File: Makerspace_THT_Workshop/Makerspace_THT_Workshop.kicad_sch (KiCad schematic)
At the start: 22 parts, among them SW1 SW_SPDT, U1 LM358, U2 LMC555xN

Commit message: Updated the board to fix alot of stuff
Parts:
- removed D2: LED, LED_THT:LED_D5.0mm_5.0mm_Pitch, symbol Device:LED
- removed R10: 100, Resistor_THT:R_Axial_DIN0207_L6.3mm_D2.5mm_P7.62mm_Horizontal, symbol Device:R
- AE1: footprint Connector_PinHeader_1.00mm:PinHeader_1x01_P1.00mm_Vertical -> TestPoint:TestPoint_Pad_D4.0mm
- BT1: footprint Battery:BatteryHolder_Keystone_3001_1x12mm -> Custom_Batteries:BK-913_MPD
- D1: footprint LED_THT:LED_D5.0mm_5.0mm_Pitch -> LED_THT:LED_D5.0mm
- R1, R2, R3, R4, R5, R6, R7, R8, R9: footprint Resistor_THT:R_Axial_DIN0207_L6.3mm_D2.5mm_P7.62mm_Horizontal -> Resistor_THT:R_Axial_DIN0207_L6.3mm_D2.5mm_P10.16mm_Horizontal
- RV1: footprint Potentiometer_THT:Potentiometer_ACP_CA9-V10_Vertical -> Custom_Potentiometer:601030_AVX
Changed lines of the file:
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@@
-	)
-	(junction
-		(at 209.55 100.33)
-		(diameter 0)
-		(color 0 0 0 0)
-	)
-	(junction
-		(at 228.6 109.22)
-		(diameter 0)
-		(color 0 0 0 0)
 	)
 	(junction
@@
 	(wire
 		(pts
-			(xy 209.55 100.33) (xy 209.55 109.22)
-		)
-		(stroke
-			(width 0)
-			(type default)
-		)
-	)
-	(wire
-		(pts
 			(xy 60.96 80.01) (xy 176.53 80.01)
 		)
@@
 	(wire
 		(pts
-			(xy 228.6 109.22) (xy 228.6 114.3)
-		)
-		(stroke
-			(width 0)
-			(type default)
-		)
-	)
-	(wire
-		(pts
 			(xy 217.17 100.33) (xy 219.71 100.33)
 		)
@@
 	(wire
 		(pts
-			(xy 227.33 109.22) (xy 228.6 109.22)
-		)
-		(stroke
-			(width 0)
-			(type default)
-		)
-	)
-	(wire
-		(pts
 			(xy 227.33 100.33) (xy 228.6 100.33)
 		)
@@
 	(wire
 		(pts
-			(xy 217.17 109.22) (xy 219.71 109.22)
-		)
-		(stroke
-			(width 0)
-			(type default)
-		)
-	)
-	(wire
-		(pts
 			(xy 110.49 90.17) (xy 114.3 90.17)
 		)
@@
 	(wire
 		(pts
-			(xy 228.6 100.33) (xy 228.6 109.22)
+			(xy 228.6 100.33) (xy 228.6 114.3)
 		)
 		(stroke
@@
 			)
 		)
-		(property "Footprint" "Potentiometer_THT:Potentiometer_ACP_CA9-V10_Vertical"
+		(property "Footprint" "Custom_Potentiometer:601030_AVX"
 			(at 100.33 102.87 0)
 			(effects
@@
 			)
 		)
-		(property "Footprint" "Resistor_THT:R_Axial_DIN0207_L6.3mm_D2.5mm_P7.62mm_Horizontal"
+		(property "Footprint" "Resistor_THT:R_Axial_DIN0207_L6.3mm_D2.5mm_P10.16mm_Horizontal"
 			(at 148.59 103.378 90)
 			(effects
@@
 			)
 		)
-		(property "Footprint" "Resistor_THT:R_Axial_DIN0207_L6.3mm_D2.5mm_P7.62mm_Horizontal"
+		(property "Footprint" "Resistor_THT:R_Axial_DIN0207_L6.3mm_D2.5mm_P10.16mm_Horizontal"
 			(at 120.65 91.948 90)
 			(effects
@@
 			)
 		)
-		(property "Footprint" "Resistor_THT:R_Axial_DIN0207_L6.3mm_D2.5mm_P7.62mm_Horizontal"
+		(property "Footprint" "Resistor_THT:R_Axial_DIN0207_L6.3mm_D2.5mm_P10.16mm_Horizontal"
 			(at 68.072 91.44 90)
 			(effects
@@
 			)
 		)
-		(property "Footprint" "Connector_PinHeader_1.00mm:PinHeader_1x01_P1.00mm_Vertical"
+		(property "Footprint" "TestPoint:TestPoint_Pad_D4.0mm"
 			(at 69.85 64.77 0)
 			(effects
@@
 			)
 		)
-		(property "Footprint" "Battery:BatteryHolder_Keystone_3001_1x12mm"
+		(property "Footprint" "Custom_Batteries:BK-913_MPD"
 			(at 48.26 97.536 90)
 			(effects
@@
 			)
 		)
-		(property "Footprint" "Resistor_THT:R_Axial_DIN0207_L6.3mm_D2.5mm_P7.62mm_Horizontal"
+		(property "Footprint" "Resistor_THT:R_Axial_DIN0207_L6.3mm_D2.5mm_P10.16mm_Horizontal"
 			(at 78.74 104.648 90)
 			(effects
@@
 			)
 		)
-		(property "Footprint" "Resistor_THT:R_Axial_DIN0207_L6.3mm_D2.5mm_P7.62mm_Horizontal"
+		(property "Footprint" "Resistor_THT:R_Axial_DIN0207_L6.3mm_D2.5mm_P10.16mm_Horizontal"
 			(at 197.612 96.52 90)
 			(effects
@@
 	)
 	(symbol
-		(lib_id "Device:R")
-		(at 213.36 109.22 90)
-		(unit 1)
-		(exclude_from_sim no)
-		(in_bom yes)
-		(on_board yes)
-		(dnp no)
-		(property "Reference" "R10"
-			(at 213.36 104.394 90)
-			(effects
-				(font
-					(size 1.27 1.27)
-				)
-			)
-		)
-		(property "Value" "100"
-			(at 213.36 106.934 90)
-			(effects
-				(font
-					(size 1.27 1.27)
-				)
-			)
-		)
-		(property "Footprint" "Resistor_THT:R_Axial_DIN0207_L6.3mm_D2.5mm_P7.62mm_Horizontal"
-			(at 213.36 110.998 90)
-			(effects
-				(font
-					(size 1.27 1.27)
-				)
-				(hide yes)
-			)
-		)
-		(property "Datasheet" "~"
-			(at 213.36 109.22 0)
-			(effects
-				(font
-					(size 1.27 1.27)
-				)
-				(hide yes)
-			)
-		)
-		(property "Description" "Resistor"
-			(at 213.36 109.22 0)
-			(effects
-				(font
-					(size 1.27 1.27)
-				)
-				(hide yes)
-			)
-		)
-		(pin "1"
-		)
-		(pin "2"
-		)
-		(instances
-			(project "Makerspace_THT_Workshop"
-				(path "/5883041f-9a7b-4515-b6ee-89cbb07e7cdb"
-					(reference "R10")
-					(unit 1)
-				)
-			)
-		)
-	)
-	(symbol
 		(lib_id "Device:C")
 		(at 127 102.87 180)
@@
 			)
 		)
-		(property "Footprint" "Resistor_THT:R_Axial_DIN0207_L6.3mm_D2.5mm_P7.62mm_Horizontal"
+		(property "Footprint" "Resistor_THT:R_Axial_DIN0207_L6.3mm_D2.5mm_P10.16mm_Horizontal"
 			(at 137.922 105.41 90)
 			(effects
@@
 			)
 		)
-		(property "Footprint" "Resistor_THT:R_Axial_DIN0207_L6.3mm_D2.5mm_P7.62mm_Horizontal"
+		(property "Footprint" "Resistor_THT:R_Axial_DIN0207_L6.3mm_D2.5mm_P10.16mm_Horizontal"
 			(at 213.36 102.108 90)
 			(effects
@@
 			)
 		)
-		(property "Footprint" "Resistor_THT:R_Axial_DIN0207_L6.3mm_D2.5mm_P7.62mm_Horizontal"
+		(property "Footprint" "Resistor_THT:R_Axial_DIN0207_L6.3mm_D2.5mm_P10.16mm_Horizontal"
 			(at 88.9 104.648 90)
 			(effects
@@
 			)
 		)
-		(property "Footprint" "Resistor_THT:R_Axial_DIN0207_L6.3mm_D2.5mm_P7.62mm_Horizontal"
+		(property "Footprint" "Resistor_THT:R_Axial_DIN0207_L6.3mm_D2.5mm_P10.16mm_Horizontal"
 			(at 112.522 102.87 90)
 			(effects
@@
 	)
 	(symbol
-		(lib_id "Device:LED")
-		(at 223.52 109.22 180)
-		(unit 1)
-		(exclude_from_sim no)
-		(in_bom yes)
-		(on_board yes)
-		(dnp no)
-		(property "Reference" "D2"
-			(at 219.964 104.394 0)
-			(effects
-				(font
-					(size 1.27 1.27)
-				)
-			)
-		)
-		(property "Value" "LED"
-			(at 219.964 106.934 0)
-			(effects
-				(font
-					(size 1.27 1.27)
-				)
-			)
-		)
-		(property "Footprint" "LED_THT:LED_D5.0mm_5.0mm_Pitch"
-			(at 223.52 109.22 0)
-			(effects
-				(font
-					(size 1.27 1.27)
-				)
-				(hide yes)
-			)
-		)
-		(property "Datasheet" "~"
-			(at 223.52 109.22 0)
-			(effects
-				(font
-					(size 1.27 1.27)
-				)
-				(hide yes)
-			)
-		)
-		(property "Description" "Light emitting diode"
-			(at 223.52 109.22 0)
-			(effects
-				(font
-					(size 1.27 1.27)
-				)
-				(hide yes)
-			)
-		)
-		(pin "1"
-		)
-		(pin "2"
-		)
-		(instances
-			(project "Makerspace_THT_Workshop"
-				(path "/5883041f-9a7b-4515-b6ee-89cbb07e7cdb"
-					(reference "D2")
-					(unit 1)
-				)
-			)
-		)
-	)
-	(symbol
 		(lib_id "Timer:LMC555xN")
 		(at 176.53 95.25 0)
@@
 			)
 		)
-		(property "Footprint" "LED_THT:LED_D5.0mm_5.0mm_Pitch"
+		(property "Footprint" "LED_THT:LED_D5.0mm"
 			(at 223.52 100.33 0)
 			(effects

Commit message: New Version of the PCB layout
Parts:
- D1: footprint LED_THT:LED_D5.0mm -> LED_THT:LED_D5.0mm_5.0mm_Pitch
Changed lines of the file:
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@@
 			)
 		)
-		(property "Footprint" "LED_THT:LED_D5.0mm"
+		(property "Footprint" "LED_THT:LED_D5.0mm_5.0mm_Pitch"
 			(at 223.52 100.33 0)
 			(effects

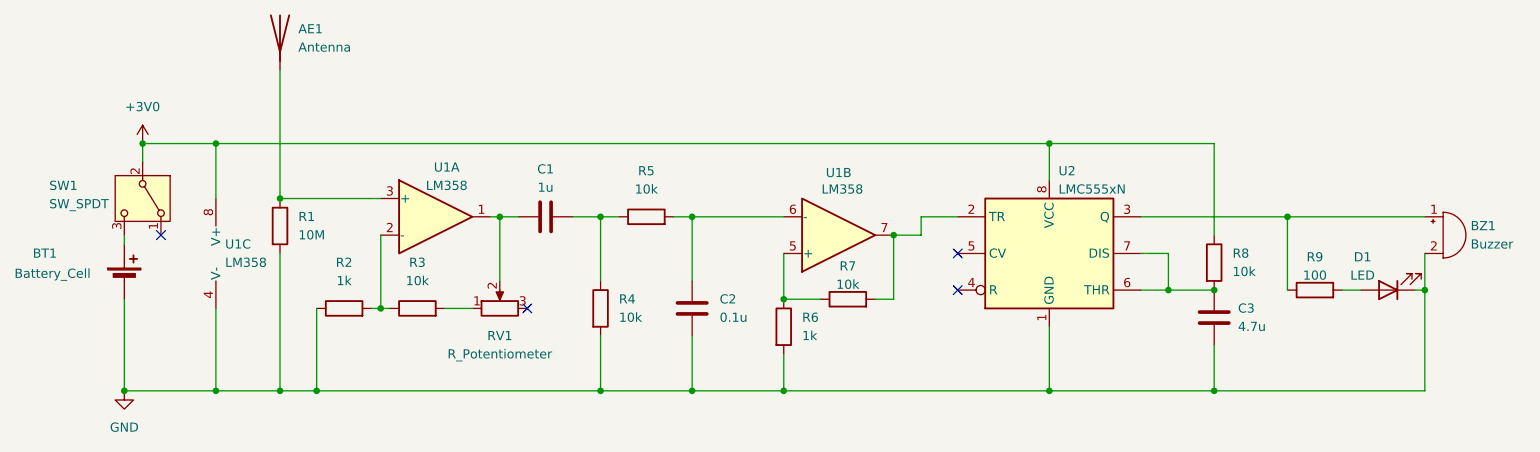
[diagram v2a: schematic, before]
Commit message: Updated PCB layout, vectors, and updated references
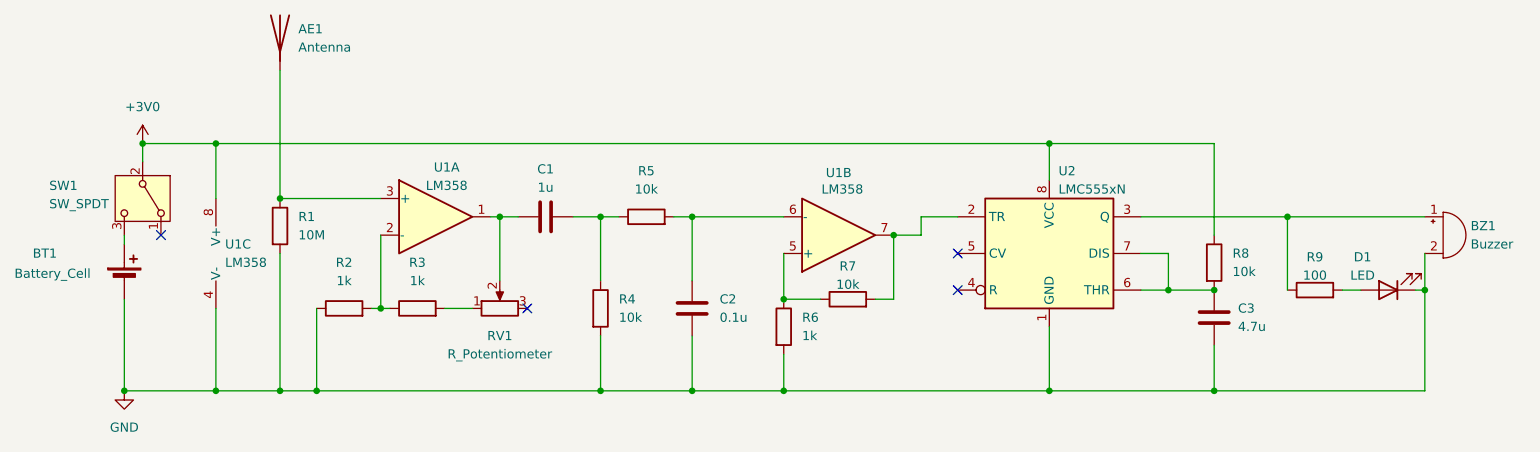
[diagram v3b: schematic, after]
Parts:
- R3: value 10k -> 1k
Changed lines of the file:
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@@
 (kicad_sch
-	(version 20231120)
+	(version 20250114)
 	(generator "eeschema")
-	(generator_version "8.0")
+	(generator_version "9.0")
 	(paper "A4")
 	(title_block
@@
 			)
 		)
-		(property "Value" "10k"
+		(property "Value" "1k"
 			(at 88.9 99.06 90)
 			(effects
@@
 		)
 	)
+	(embedded_fonts no)
 )
